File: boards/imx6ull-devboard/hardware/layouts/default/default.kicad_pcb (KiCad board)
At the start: 2 copper layers, 0 parts

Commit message: Ethernet subsystem v0 — wired + reviewed
- src/network.ato: LAN8742A wrapper consuming the atopile package, plus wrapper-level
  fixes for two CRITICAL bugs the reviewer agent caught in atopile/microchip-lan8742a@0.3.0:
    * nINTSEL strap pulldown (4.75kΩ) so PHY drives 50MHz REF_CLK to MAC at boot
    * MDI termination (4× 49.9Ω 1% on TXP/TXN/RXP/RXN to VDDA) per Microchip Checklist
  Plus: 1.5kΩ MDIO pullup (IEEE 802.3 open-drain), MDC pullup removed (push-pull).
- src/main.ato: Network module wired in; restructured paths.src to ./src.
- docs/subsystems/{README,ethernet}.md: design doc with reviewer findings table,
  open TODOs for HR911105A magjack + Bob Smith + ESD + crystal cap upstream PR.
- ato.yaml: added atopile/microchip-lan8742a@0.3.0 dep; entry path updated.

Build clean (5s), 13-line BOM picked. 5/10 issues fixed; 5 deferred to follow-up
(magjack wrapper, upstream PR, Debug subsystem).

Co-Authored-By: Claude Opus 4.7 (1M context) <noreply@anthropic.com>
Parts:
- added C1: 100nF ±10%, Samsung_Electro_Mechanics_CL05B104KO5NNNC:C0402, F.Cu at (2.14, -2.99)
- added C2: 100nF ±10%, Samsung_Electro_Mechanics_CL05B104KO5NNNC:C0402, F.Cu at (-2.53, -3.52)
- added C3: 100nF ±10%, Samsung_Electro_Mechanics_CL05B104KO5NNNC:C0402, F.Cu at (-0.22, 4.22)
- added C4: 100nF ±10%, Samsung_Electro_Mechanics_CL05B104KO5NNNC:C0402, F.Cu at (2.15, -4.00)
- added C5: 1µF ±10%, Samsung_Electro_Mechanics_CL05A105KA5NQNC:C0402, F.Cu at (2.14, -2.99)
- added C6: 1µF ±10%, Samsung_Electro_Mechanics_CL05A105KA5NQNC:C0402, F.Cu at (-3.08, 3.35)
- added C7: 470pF ±10%, FH_0402B471K500NT:C0402, F.Cu at (-3.10, 4.27)
- added C8: 18pF ±5%, FH_0402CG180J500NT:C0402, F.Cu at (-5.53, 3.31)
- added C9: 18pF ±5%, FH_0402CG180J500NT:C0402, F.Cu at (-5.50, -1.90)
- added R1: 4.75kΩ ±1%, UNI_ROYAL_0402WGF4751TCE:R0402, F.Cu at (0.00, 0.00)
- added R10: 49.9Ω ±1%, UNI_ROYAL_0402WGF499JTCE:R0402, F.Cu at (0.00, -40.0)
- added R2: 1.5kΩ ±1%, UNI_ROYAL_0402WGF1501TCE:R0402, F.Cu at (20.0, -10.0)
- added R3: 100kΩ ±1%, UNI_ROYAL_0402WGF1003TCE:R0402, F.Cu at (0.79, 4.10)
- added R4: 12.1kΩ ±1%, YAGEO_RC0402FR_0712K1L:R0402, F.Cu at (-1.55, -3.72)
- added R5: 100kΩ ±1%, UNI_ROYAL_0402WGF1003TCE:R0402, F.Cu at (-5.34, -2.90)
- added R6: 10kΩ ±1%, UNI_ROYAL_0402WGF1002TCE:R0402, F.Cu at (3.54, 0.24)
- added R7: 49.9Ω ±1%, UNI_ROYAL_0402WGF499JTCE:R0402, F.Cu at (0.00, -10.0)
- added R8: 49.9Ω ±1%, UNI_ROYAL_0402WGF499JTCE:R0402, F.Cu at (0.00, -20.0)
- added R9: 49.9Ω ±1%, UNI_ROYAL_0402WGF499JTCE:R0402, F.Cu at (0.00, -30.0)
- added U1: , Microchip_Tech_LAN8742A_CZ_TR:QFN-24_L4.0-W4.0-P0.50-TL-EP2.5, F.Cu at (0.00, 0.00)
- added X1: , Yangxing_Tech_X322525MRB4SI:OSC-SMD_4P-L3.2-W2.5-BL_SIT8008BI, F.Cu at (-4.95, 0.67)
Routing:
- net xtal_caps[1]-power-hv: track 0.00 -> 5.98 mm
- net 2: track 0.00 -> 5.77 mm
- net lv: track 0.00 -> 4.49 mm
- net xtal_caps[0]-power-hv: track 0.00 -> 4.43 mm
- net 0: track 0.00 -> 4.27 mm
- net vddcr_caps[1]-power-hv: track 0.00 -> 3.70 mm
- net phy-rmii-line: track 0.00 -> 1.89 mm
- net RBIAS: track 0.00 -> 1.41 mm
- net line: track 0.00 -> 1.11 mm

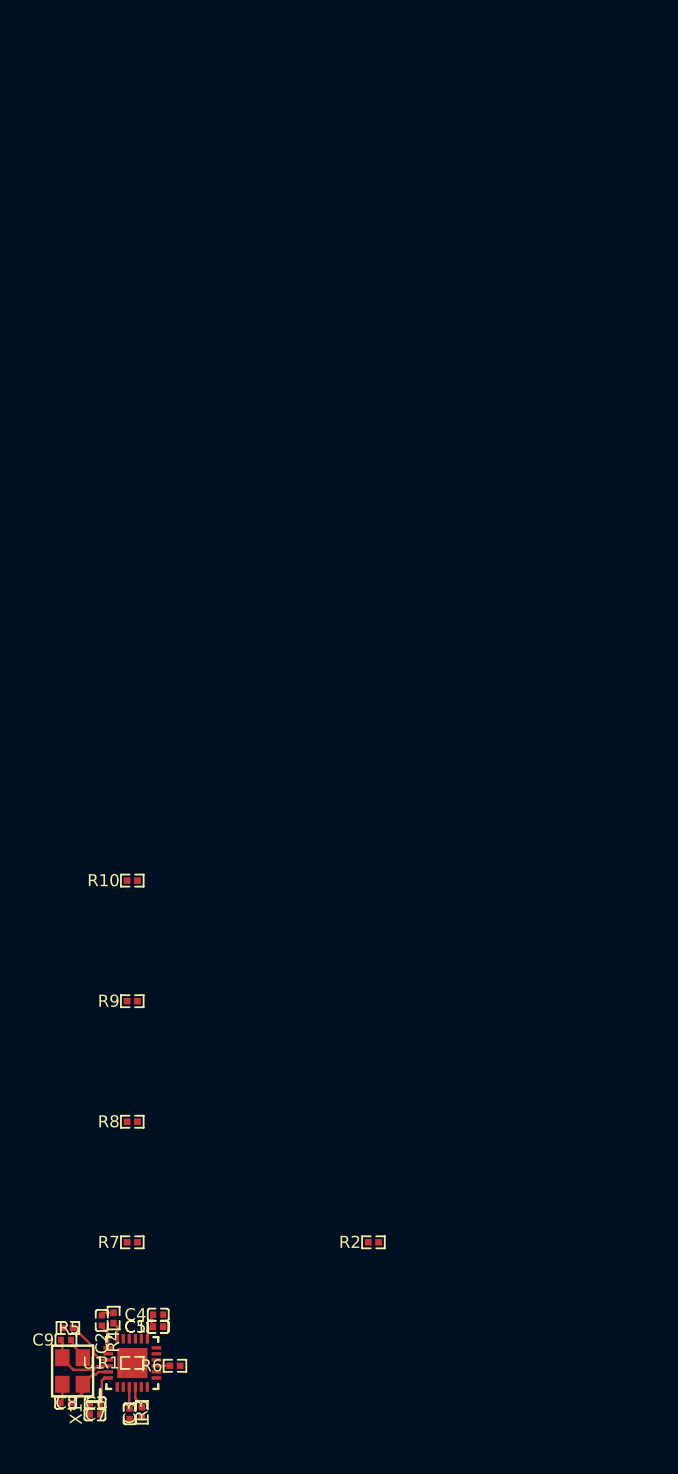
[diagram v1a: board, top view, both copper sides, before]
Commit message: Power Tree subsystem v0 — wired + reviewed (6 fixes applied)
Subsystems: 3x TPS563201 buck (3V3, 1V4, 1V35) + TLV75901 LDO (1V8) + LDK220 LDO
(SNVS) with reviewer-driven fixes:

  * EN-pin RC delay caps (470nF) so SNVS LDO comes up before any buck soft-start
  * Coin-cell OR'd into power_snvs via 2x SS34 Schottkys with vbat_in interface
  * Ferrite bead split between VDDARM and VDDSOC (NXP HDG §4.2)
  * Ferrite bead + 22µF bulk on NVCC_DRAM output (DDR3L ripple budget)
  * Inductor saturation requirement bumped to ≥4.5A (above OCL peak)
  * 1V35 setpoint tightened to ±4% (DDR3L Vddq abs-max headroom)

Deferred reviewer items:
  - 5V inrush control → Power Input subsystem
  - Multi-rail PG supervisor → Debug subsystem
  - FB ripple injection on TPS563201 → upstream PR
  - VTT termination → DDR3 subsystem (TPS51200 needs `ato create part`)

Build clean (21s), 31-line BOM, 3x TPS563201 + 2x ferrite + 2x Schottky commonized.

Co-Authored-By: Claude Opus 4.7 (1M context) <noreply@anthropic.com>
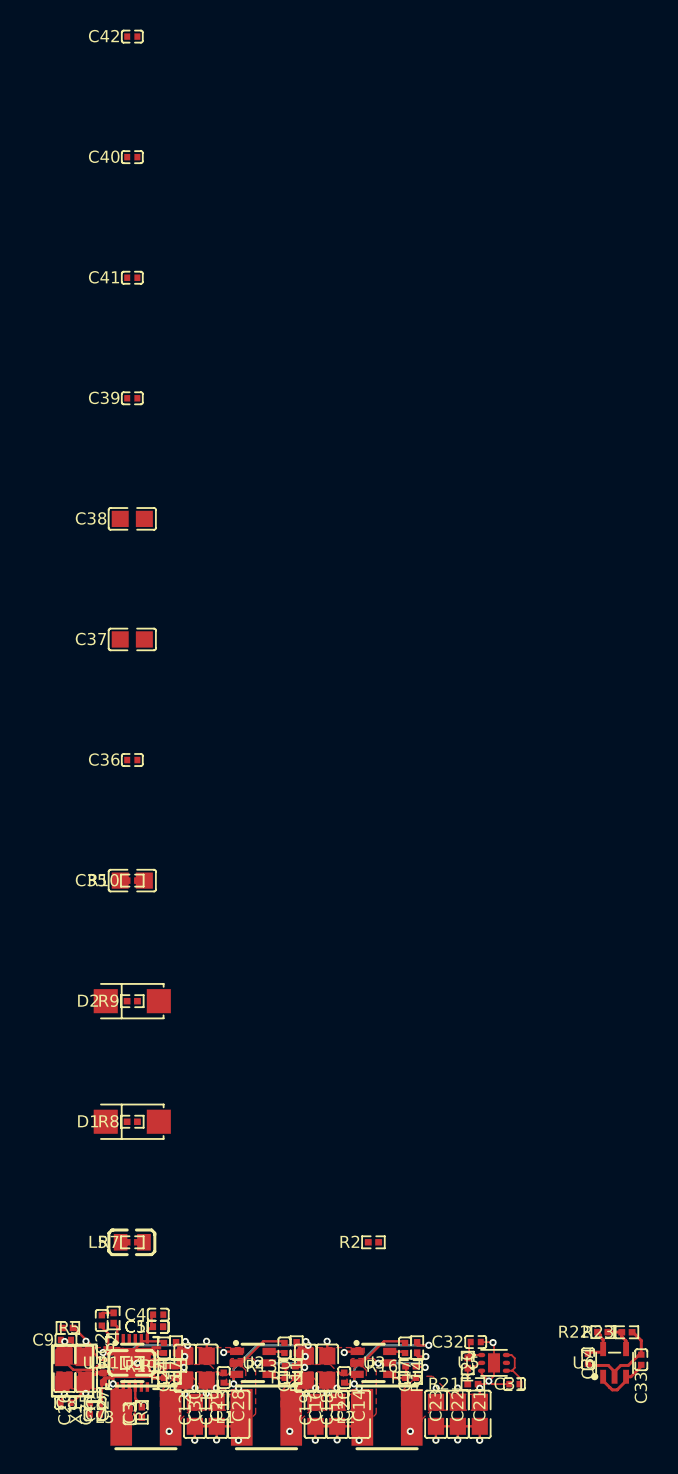
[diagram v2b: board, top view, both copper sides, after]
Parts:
- added C10: 100nF ±10%, Samsung_Electro_Mechanics_CL05B104KO5NNNC:C0402, F.Cu at (12.6, -1.24)
- added C11: 10µF ±10%, Samsung_Electro_Mechanics_CL21A106KAYNNNE:C0805, F.Cu at (6.17, 0.43)
- added C12: 10µF ±10%, Samsung_Electro_Mechanics_CL21A106KAYNNNE:C0805, F.Cu at (4.39, 0.45)
- added C13: 100nF ±10%, Samsung_Electro_Mechanics_CL05B104KO5NNNC:C0402, F.Cu at (7.58, 1.22)
- added C14: 10µF ±10%, Samsung_Electro_Mechanics_CL21A106KAYNNNE:C0805, F.Cu at (18.8, 4.26)
- added C15: 10µF ±10%, Samsung_Electro_Mechanics_CL21A106KAYNNNE:C0805, F.Cu at (17.0, 4.26)
- added C16: 10µF ±10%, Samsung_Electro_Mechanics_CL21A106KAYNNNE:C0805, F.Cu at (15.2, 4.26)
- added C17: 100nF ±10%, Samsung_Electro_Mechanics_CL05B104KO5NNNC:C0402, F.Cu at (22.6, -1.24)
- added C18: 10µF ±10%, Samsung_Electro_Mechanics_CL21A106KAYNNNE:C0805, F.Cu at (16.2, 0.43)
- added C19: 10µF ±10%, Samsung_Electro_Mechanics_CL21A106KAYNNNE:C0805, F.Cu at (14.4, 0.45)
- added C20: 100nF ±10%, Samsung_Electro_Mechanics_CL05B104KO5NNNC:C0402, F.Cu at (17.6, 1.22)
- added C21: 10µF ±10%, Samsung_Electro_Mechanics_CL21A106KAYNNNE:C0805, F.Cu at (28.8, 4.26)
- added C22: 10µF ±10%, Samsung_Electro_Mechanics_CL21A106KAYNNNE:C0805, F.Cu at (27.0, 4.26)
- added C23: 10µF ±10%, Samsung_Electro_Mechanics_CL21A106KAYNNNE:C0805, F.Cu at (25.2, 4.26)
- added C24: 100nF ±10%, Samsung_Electro_Mechanics_CL05B104KO5NNNC:C0402, F.Cu at (2.62, -1.24)
- added C25: 10µF ±10%, Samsung_Electro_Mechanics_CL21A106KAYNNNE:C0805, F.Cu at (-3.83, 0.43)
- added C26: 10µF ±10%, Samsung_Electro_Mechanics_CL21A106KAYNNNE:C0805, F.Cu at (-5.61, 0.45)
- added C27: 100nF ±10%, Samsung_Electro_Mechanics_CL05B104KO5NNNC:C0402, F.Cu at (-2.42, 1.22)
- added C28: 10µF ±10%, Samsung_Electro_Mechanics_CL21A106KAYNNNE:C0805, F.Cu at (8.82, 4.26)
- added C29: 10µF ±10%, Samsung_Electro_Mechanics_CL21A106KAYNNNE:C0805, F.Cu at (7.00, 4.26)
- added C30: 10µF ±10%, Samsung_Electro_Mechanics_CL21A106KAYNNNE:C0805, F.Cu at (5.19, 4.26)
- added C31: 1µF ±10%, Samsung_Electro_Mechanics_CL05A105KA5NQNC:C0402, F.Cu at (31.7, 1.76)
- added C32: 1µF ±10%, Samsung_Electro_Mechanics_CL05A105KA5NQNC:C0402, F.Cu at (28.5, -1.73)
- added C33: 1µF ±10%, Samsung_Electro_Mechanics_CL05A105KA5NQNC:C0402, F.Cu at (42.2, -0.26)
- added C34: 1µF ±10%, Samsung_Electro_Mechanics_CL05A105KA5NQNC:C0402, F.Cu at (37.8, -0.34)
- added C35: 22µF ±20%, Samsung_Electro_Mechanics_CL21A226MAQNNNE:C0805, F.Cu at (0.00, -40.0)
- added C36: 100nF ±10%, Samsung_Electro_Mechanics_CL05B104KO5NNNC:C0402, F.Cu at (0.00, -50.0)
- added C37: 10µF ±10%, Samsung_Electro_Mechanics_CL21A106KAYNNNE:C0805, F.Cu at (0.00, -60.0)
- added C38: 10µF ±10%, Samsung_Electro_Mechanics_CL21A106KAYNNNE:C0805, F.Cu at (0.00, -70.0)
- added C39: 100nF ±10%, Samsung_Electro_Mechanics_CL05B104KO5NNNC:C0402, F.Cu at (0.00, -80.0)
- added C40: 470nF ±10%, Samsung_Electro_Mechanics_CL05A474KP5NNNC:C0402, F.Cu at (0.00, -100.0)
- added C41: 470nF ±10%, Samsung_Electro_Mechanics_CL05A474KP5NNNC:C0402, F.Cu at (0.00, -90.0)
- added C42: 470nF ±10%, Samsung_Electro_Mechanics_CL05A474KP5NNNC:C0402, F.Cu at (0.00, -110.0)
- added D1: Vf {ℝ+}V, MDD_Microdiode_Electronics_SS34:SMA_L4.3-W2.6-LS5.2-RD, F.Cu at (0.00, -20.0)
- added D2: Vf {ℝ+}V, MDD_Microdiode_Electronics_SS34:SMA_L4.3-W2.6-LS5.2-RD, F.Cu at (0.00, -30.0)
- added L1: L 1.54-2.86µH, SXN_SMNR5030_2R2N:IND-SMD_L5.0-W5.0_SMNR5030, F.Cu at (11.1, 4.52)
- added L2: L 1.54-2.86µH, SXN_SMNR5030_2R2N:IND-SMD_L5.0-W5.0_SMNR5030, F.Cu at (21.1, 4.52)
- added L3: L 1.54-2.86µH, SXN_SMNR5030_2R2N:IND-SMD_L5.0-W5.0_SMNR5030, F.Cu at (1.13, 4.52)
- added L4: L {ℝ+}H, Sunlord_GZ2012D601TF:L0805, F.Cu at (0.00, 0.00)
- added L5: L {ℝ+}H, Sunlord_GZ2012D601TF:L0805, F.Cu at (0.00, -10.0)
- added R11: 10kΩ ±1%, UNI_ROYAL_0402WGF1002TCE:R0402, F.Cu at (13.6, -1.27)
- added R12: 13.3kΩ ±1%, FOJAN_FRC0402F1332TS:R0402, F.Cu at (13.1, 1.24)
- added R13: 16.2kΩ ±1%, UNI_ROYAL_0402WGF1622TCE:R0402, F.Cu at (13.1, 0.28)
- added R14: 10kΩ ±1%, UNI_ROYAL_0402WGF1002TCE:R0402, F.Cu at (23.6, -1.27)
- added R15: 16.2kΩ ±1%, UNI_ROYAL_0402WGF1622TCE:R0402, F.Cu at (23.1, 1.24)
- added R16: 21.5kΩ ±1%, UNI_ROYAL_0402WGF2152TCE:R0402, F.Cu at (23.1, 0.28)
- added R17: 10kΩ ±1%, UNI_ROYAL_0402WGF1002TCE:R0402, F.Cu at (3.63, -1.27)
- added R18: 10.2kΩ ±1%, UNI_ROYAL_0402WGF1022TCE:R0402, F.Cu at (3.09, 1.24)
- added R19: 3.09kΩ ±1%, Viking_Tech_ARG02FTC3091:R0402, F.Cu at (3.10, 0.28)
- added R20: 6.34kΩ ±0.1%, YAGEO_RT0402BRE076K34L:R0402, F.Cu at (27.8, 0.01)
- added R21: 2.8kΩ ±1%, FOJAN_FRC0402F2801TS:R0402, F.Cu at (28.2, 1.76)
- added R22: 13.7kΩ ±1%, UNI_ROYAL_0402WGF1372TCE:R0402, F.Cu at (39.0, -2.55)
- added R23: 16.9kΩ ±1%, UNI_ROYAL_0402WGF1692TCE:R0402, F.Cu at (41.0, -2.54)
- added U2: , Texas_Instruments_TPS563201DDCR:SOT-23-6_L2.9-W1.6-P0.95-LS2.8-BR, F.Cu at (10.0, 0.00)
- added U3: , Texas_Instruments_TPS563201DDCR:SOT-23-6_L2.9-W1.6-P0.95-LS2.8-BR, F.Cu at (20.0, 0.00)
- added U4: , Texas_Instruments_TPS563201DDCR:SOT-23-6_L2.9-W1.6-P0.95-LS2.8-BR, F.Cu at (0.00, 0.00)
- added U5: , Texas_Instruments_TLV75901PDRVR:WSON-6_L2.0-W2.0-P0.65-TL-EP, F.Cu at (30.0, 0.00)
- added U6: , STMicroelectronics_LDK220M_R:SOT-23-5_L3.0-W1.7-P0.95-LS2.8-BL, F.Cu at (40.0, 0.00)
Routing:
- net 0: track 4.27 -> 81.9 mm, vias 0 -> 24
- net lv: track 4.49 -> 56.2 mm, vias 0 -> 23
- net 15: track 0.00 -> 5.89 mm, vias 0 -> 2
- net 35: track 0.00 -> 5.89 mm, vias 0 -> 2
- net 38: track 0.00 -> 5.89 mm, vias 0 -> 2
- net 2: track 5.77 -> 0.00 mm
- net power_5v-hv: track 0.00 -> 4.83 mm
- net en_delay_1v35-power-hv: track 0.00 -> 4.49 mm
- net hv: track 0.00 -> 3.86 mm
- net power_1v8-hv: track 0.00 -> 2.74 mm
- net feedback_divider-ref_out-hv-3: track 0.00 -> 2.65 mm
- added copper zone on F.Cu, net 0
- added copper zone on F.Cu, net lv

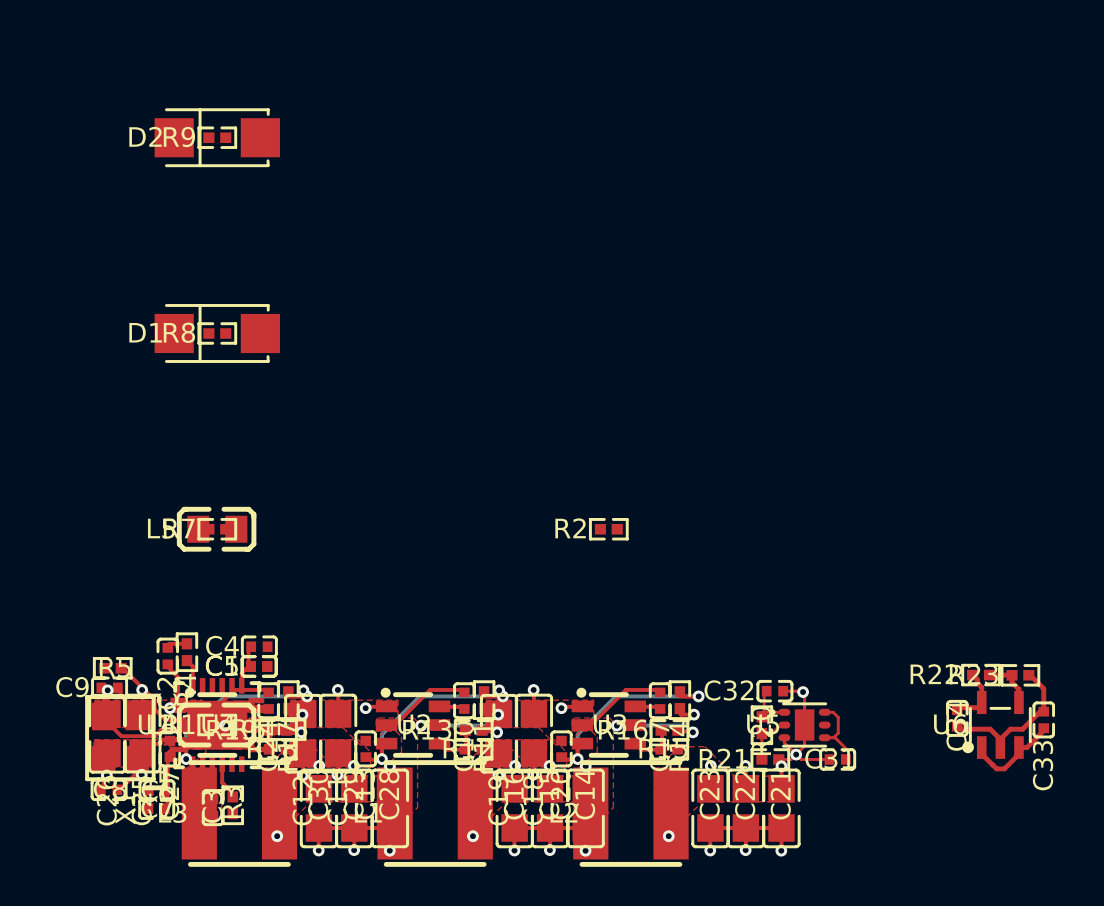
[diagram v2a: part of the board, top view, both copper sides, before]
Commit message: USB-UART subsystem v0 — CH340N → USB-C #3
CH340N (SOP-8, $0.48) USB-to-UART bridge for board console. Powered from 5V_BOARD
(simpler than VBUS, avoids backfeed). USB-C #3 (TYPE-C-31-M-17, commonized with
PD #1 and OTG #2). 33Ω series on TX/RX for edge-rate slowing + accidental-short
current limit.

Generated WCH_CH340N atomic part via `ato create part --search C2977777` —
first use of that flow in the project. Flow worked cleanly.

TODO (deferred to Debug subsystem): 4-pin TTL header tapped to same UART1 lines
for users with their own USB-TTL dongle.

Co-Authored-By: Claude Opus 4.7 (1M context) <noreply@anthropic.com>
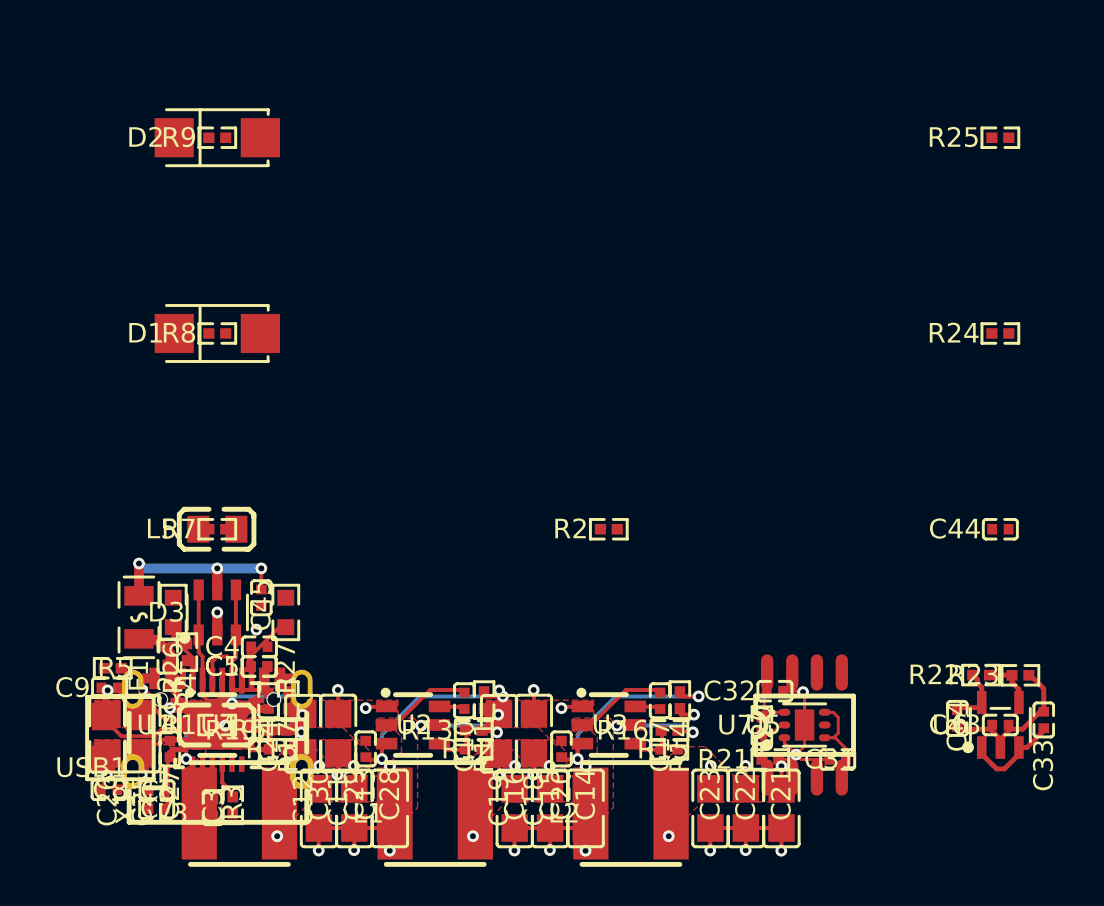
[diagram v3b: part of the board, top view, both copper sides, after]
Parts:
- added C43: 100nF ±10%, Samsung_Electro_Mechanics_CL05B104KO5NNNC:C0402, F.Cu at (40.0, 0.00)
- added C44: 100nF ±10%, Samsung_Electro_Mechanics_CL05B104KO5NNNC:C0402, F.Cu at (40.0, -10.0)
- added C45: 100nF ±10%, Samsung_Electro_Mechanics_CL05B104KO5NNNC:C0402, F.Cu at (2.25, -6.50)
- added D3: , STMicroelectronics_USBLC6_2SC6:SOT-23-6_L2.9-W1.6-P0.95-LS2.8-BL, F.Cu at (0.00, -5.75)
- added F1: , BHFUSE_BSMD0805_050_15V:F0805, F.Cu at (-4.00, -5.50)
- added R24: 33Ω ±1%, UNI_ROYAL_0402WGF330JTCE:R0402, F.Cu at (40.0, -20.0)
- added R25: 33Ω ±1%, UNI_ROYAL_0402WGF330JTCE:R0402, F.Cu at (40.0, -30.0)
- added R26: 10kΩ ±1%, UNI_ROYAL_0603WAF1002T5E:R0603, F.Cu at (-2.25, -5.75)
- added R27: 10kΩ ±1%, UNI_ROYAL_0603WAF1002T5E:R0603, F.Cu at (3.50, -5.75)
- added U7: , WCH_CH340N:SOP-8_L4.9-W3.9-P1.27-LS6.0-BL, F.Cu at (30.0, 0.00)
- added USB1: , SHOU_HAN_TYPE_C_16PIN_2MD_073:USB-C-SMD_TYPE-C-6PIN-2MD-073, F.Cu at (0.00, 0.00)
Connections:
- C1 pad 1: hv -> power_3v3-hv
- C2 pad 1: hv -> power_3v3-hv
- C28 pad 1: hv -> power_3v3-hv
- C29 pad 1: hv -> power_3v3-hv
- C3 pad 1: hv -> power_3v3-hv
- C30 pad 1: hv -> power_3v3-hv
- C31 pad 1: hv -> power_3v3-hv
- C4 pad 1: hv -> power_3v3-hv
- C5 pad 1: hv -> power_3v3-hv
- L1 pad 1: (no net) -> bootstrap_cap-power-lv-1
- L1 pad 2: (no net) -> power_1v4_arm-hv
- L2 pad 1: (no net) -> bootstrap_cap-power-lv
- L2 pad 2: (no net) -> _buck_1v35_out-hv
- L3 pad 1: (no net) -> bootstrap_cap-power-lv-2
- L3 pad 2: (no net) -> power_3v3-hv
- R10 pad 2: hv -> power_3v3-hv
- R18 pad 1: hv -> power_3v3-hv
- R2 pad 2: hv -> power_3v3-hv
- R6 pad 2: hv -> power_3v3-hv
- R7 pad 2: hv -> power_3v3-hv
- R8 pad 2: hv -> power_3v3-hv
- R9 pad 2: hv -> power_3v3-hv
- U1 pad 1: hv -> power_3v3-hv
- U1 pad 19: hv -> power_3v3-hv
- U1 pad 9: hv -> power_3v3-hv
- U5 pad 4: hv -> power_3v3-hv
- U5 pad 6: hv -> power_3v3-hv
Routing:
- net 2: track 0.00 -> 56.2 mm, vias 0 -> 23
- net lv: track 56.2 -> 10.6 mm, vias 23 -> 0
- net 0: track 81.9 -> 92.7 mm, vias 24 -> 27
- net 10: track 0.00 -> 10.0 mm, vias 0 -> 3
- net DATA_N: track 0.00 -> 7.57 mm
- net DATA_P: track 0.00 -> 6.68 mm
- net 15: track 5.89 -> 0.00 mm, vias 2 -> 0
- net nRTS: track 0.00 -> 5.89 mm, vias 0 -> 2
- net 35: track 5.89 -> 0.00 mm, vias 2 -> 0
- net TXD: track 0.00 -> 5.89 mm, vias 0 -> 2
- net 38: track 5.89 -> 0.00 mm, vias 2 -> 0
- net power_5v-hv: track 4.83 -> 0.00 mm
- net 12: track 0.00 -> 4.83 mm
- net power_3v3-hv: track 0.00 -> 3.86 mm
- net hv: track 3.86 -> 5.89 mm, vias 0 -> 2
